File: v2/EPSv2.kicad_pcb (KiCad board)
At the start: 4 copper layers, 50 x 110 mm, 155 parts, among them J1 Conn_01x02, J10 Conn_01x05_Pin, J2 Conn_01x03, J3 Conn_01x03, J4 5037630491, J5 2P 21700 Cell Holder, J6 5037630491, J7 1053091102, J8 1053091102, J9 1053091102, Q1 AO3400A, Q2 AO3400A, Q3 AO3400A, Q4 AO3400A, Q5 AP25P06K, Q6 AP25P06K, Q7 AP25P06K, U1 BQ29700DSER, U10 C3235556 (M66200DRLR), U11 C3235556 (M66200DRLR), U12 TPS63070RNMR, U13 TPS63070RNMR, U14 20m 1206, U15 INA199A1DCKR, U16 20m 1206, U17 INA199A1DCKR, U18 20m 1206, U19 INA199A1DCKR, U2 BQ29700DSER, U20 TPS63070RNMR, U3 MCP73831T-2ACI/OT, U4 MCP73831T-2ACI/OT, U6 C3235556 (M66200DRLR), U7 C3235556 (M66200DRLR), U8 C3235556 (M66200DRLR), U9 STM32L432KCUx

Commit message: preliminary layout
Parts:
- moved L1 202.9 mm to (-11.8, -3.02)
- moved C1 202.9 mm to (-13.9, 2.40)
- moved C10 202.9 mm to (-9.86, 13.1)
- moved C2 202.9 mm to (-13.9, 5.08)
- moved C3 202.9 mm to (-13.9, 7.76)
- moved C4 202.9 mm to (-13.9, 10.4)
- moved C5 202.9 mm to (-13.9, 13.1)
- moved C6 202.9 mm to (-9.86, 2.40)
- moved C7 202.9 mm to (-9.86, 5.08)
- moved C8 202.9 mm to (-9.86, 7.76)
- moved C9 202.9 mm to (-9.86, 10.4)
- moved TP7 139.3 mm to (-4.57, 20.2)
- moved U15 123.4 mm to (3.30, -40.9), turned to 180 degrees
- moved R1 123.4 mm to (-22.1, -10.3)
- moved R2 123.4 mm to (-22.1, -7.80)
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- renumbered J2 to J1, J3 to J2, J1 to J3, U14 to L4, U16 to L5, U18 to L6, L4 to L7, R21 to R20, R22 to R21, R23 to R22, R26 to R23, R27 to R24, R28 to R25, R29 to R26, R30 to R27, R31 to R28, R32 to R29, R33 to R30, R34 to R31, R35 to R32, R36 to R33, R37 to R34, R38 to R35, R39 to R36, R40 to R37, R41 to R38, R42 to R39, R43 to R40, R44 to R41, R45 to R42, R46 to R43, R47 to R44, R48 to R45, R49 to R46, R50 to R47, U11 to U10, U12 to U11, U13 to U12, U15 to U13, U17 to U14, U19 to U15, U20 to U16, U6 to U5, U7 to U6, U8 to U7, U9 to U8, U10 to U9
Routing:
- net PB0: track 44.6 -> 0.00 mm
- net PB1: track 43.9 -> 0.00 mm
- net GND: track 13.9 -> 0.00 mm
- net /Reverse_Polarity/VIN: track 2.24 -> 10.1 mm
- net /MCP73831_1/+5V_VIN: track 14.6 -> 21.7 mm
- net Net-(U2-BAT): track 5.77 -> 0.00 mm
- net Net-(Q4-G): track 5.59 -> 0.00 mm
- net CELL_2-: track 6.93 -> 1.75 mm
- net Net-(U16-EN): track 0.00 -> 3.80 mm
- net Net-(Q3-G): track 3.58 -> 0.00 mm
- net Net-(D1-A): track 3.97 -> 7.48 mm
- net Net-(LED6-A): track 0.00 -> 3.48 mm
- net /INA199_3/IN+: track 0.00 -> 2.50 mm
- net Net-(U16-Vaux): track 0.00 -> 2.15 mm
- net /INA199_3/IN-: track 0.00 -> 2.14 mm
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- added copper zone on F.Cu, net +5V
- added copper zone on F.Cu, net +9V
- added copper zone on F.Cu, net /INA199_1/IN+
- added copper zone on F.Cu, net /INA199_2/IN+
- added copper zone on F.Cu, net /INA199_3/IN+
- added copper zone on F.Cu, net CELL_1-
- added copper zone on F.Cu, net CELL_2-
- added copper zone on F.Cu, net Net-(Q1-D)
- added copper zone on F.Cu, net Net-(Q1-G)
- added copper zone on F.Cu, net Net-(Q2-G)
- added copper zone on F.Cu, net Net-(Q3-D)
- added copper zone on F.Cu, net Net-(Q3-G)
- added copper zone on F.Cu, net Net-(Q4-G)
- added copper zone on F.Cu, net Net-(U1-BAT)
- added copper zone on F.Cu, net Net-(U1-V-)
- added copper zone on F.Cu, net Net-(U12-FB)
- added copper zone on F.Cu, net Net-(U12-L1)
- added copper zone on F.Cu, net Net-(U12-L2)
- added copper zone on F.Cu, net Net-(U16-FB)
- added copper zone on F.Cu, net Net-(U16-L1)
- added copper zone on F.Cu, net Net-(U16-L2)
- added copper zone on F.Cu, net Net-(U2-BAT)
- added copper zone on F.Cu, net Net-(U2-V-)
- removed copper zone on F.Cu, net Net-(U11-FB)
- removed copper zone on F.Cu, net Net-(U11-L1)
- removed copper zone on F.Cu, net Net-(U11-L2)

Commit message: battery charging routing
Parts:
- removed the C10 at (-9.86, 13.1)
- removed the C3 at (-13.9, 7.76)
- removed the C4 at (-13.9, 10.4)
- removed the C5 at (-13.9, 13.1)
- removed the C6 at (-9.86, 2.40)
- removed the C7 at (-9.86, 5.08)
- removed the C8 at (-9.86, 7.76)
- removed the C9 at (-9.86, 10.4)
- added G***: LOGO, Rocketry_Manual:RocketryLogo, F.Cu at (-20.8, -26.2)
- C1, C2: value 10uF 0603 -> 47uF; footprint Rocketry_Easyeda:C0603 -> Capacitor_SMD:C_0603_1608Metric
- moved TP3 124.5 mm to (2.54, 4.06)
- moved TP4 111.7 mm to (15.0, 4.06)
- moved J10 50.4 mm to (-11.2, 51.3), turned to 90 degrees
- moved R21 45.3 mm to (15.2, 6.96), turned to 180 degrees
- moved U6 45.0 mm to (15.1, 9.25), turned to -90 degrees
- moved R20 34.0 mm to (2.55, 6.97), turned to 180 degrees
- moved U5 33.6 mm to (2.42, 9.27), turned to -90 degrees
- moved C22 23.0 mm to (-19.6, 12.1)
- moved C23 23.0 mm to (-17.8, 12.1)
- moved C25 23.0 mm to (-13.7, 18.6)
- moved C28 23.0 mm to (-11.7, 12.2)
- moved L3 23.0 mm to (-15.0, 11.6)
- moved R33 23.0 mm to (-17.8, 15.3)
- moved R35 23.0 mm to (-10.9, 15.5)
- moved R36 23.0 mm to (-15.8, 18.6)
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- renumbered C18 to C10, C19 to C11, C20 to C12, C21 to C13, C22 to C14, C23 to C15, C24 to C16, C25 to C17, C26 to C18, C27 to C19, C28 to C20, C29 to C21, C30 to C22, C31 to C23, C32 to C24, C33 to C25, C34 to C26, C35 to C27, C36 to C28, C37 to C29, C11 to C3, C38 to C30, C39 to C31, C40 to C32, C41 to C33, C42 to C34, C43 to C35, C44 to C36, C45 to C37, C46 to C38, C12 to C4, C13 to C5, C14 to C6, C15 to C7, C16 to C8, C17 to C9
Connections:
- C1 pad 1: GND -> +3.3V
- C1 pad 2: +3.3V -> GND
- C2 pad 1: GND -> /STM32L432KCUx/+3V3A
- C2 pad 2: +3.3V -> GND
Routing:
- net GND: track 0.00 -> 30.8 mm, vias 0 -> 13
- net /STM32L432KCUx/+3V3A: track 0.00 -> 11.5 mm
- net /MCP73831_1/+5V_VIN: track 21.7 -> 13.5 mm
- net /BQ29700_2/CELL+: track 4.84 -> 1.88 mm, vias 0 -> 18
- net PA0: track 0.00 -> 2.94 mm, vias 0 -> 1
- net PA1: track 0.00 -> 2.63 mm, vias 0 -> 1
- net +3.3V: track 1.74 -> 3.48 mm
- net Net-(U5-ST): track 0.00 -> 1.65 mm
- net Net-(U6-ST): track 0.00 -> 1.64 mm
- net /LM66200_2/VOUT: track 7.41 -> 8.69 mm
- net /INA199_2/IN+: track 0.00 -> 1.28 mm
- net /BQ29700_1/CELL+: track 4.84 -> 5.30 mm, vias 0 -> 18
- net CELL_2+: vias 0 -> 12
- net CELL_1+: vias 0 -> 12
- net /INA199_1/IN-: vias 0 -> 4
- added copper zone on B.Cu, net /BQ29700_1/CELL+
- added copper zone on F.Cu, net /BQ29700_1/CELL+
- added copper zone on B.Cu, net /BQ29700_2/CELL+
- added copper zone on F.Cu, net /BQ29700_2/CELL+
- added copper zone on B.Cu, net /INA199_1/IN-
- added copper zone on F.Cu, net /INA199_1/IN-
- added copper zone on F.Cu, net /MCP73831_1/+5V_VIN
- added copper zone on B.Cu, net CELL_1+
- added copper zone on B.Cu, net CELL_2+
- added copper zone on B.Cu, net GND
- added copper zone on F.Cu, net GND
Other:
- board text added: "+3.3V"
- board text added: "+9V"
- board text added: "EPS v2"
- board text added: "McMaster Rocketry"

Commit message: routing done
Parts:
- removed the C29 at (-19.3, -38.1)
- removed the C30 at (-3.32, -38.1)
- removed the L4 at (-16.5, -39.6)
- removed L5, L6: 20m 1206, Rocketry_Easyeda:R1206
- removed the R24 at (2.27, -35.5)
- removed the R25 at (10.0, -35.5)
- removed the R5 at (-16.3, -33.5)
- removed the R6 at (-0.27, -33.5)
- removed the R7 at (7.62, -33.5)
- removed the U10 at (7.49, -35.5)
- removed the U13 at (-19.3, -40.4)
- removed U14, U15: INA199A1DCKR, Rocketry_Easyeda:SC-70-6_L2.2-W1.3-P0.65-LS2.1-BR
- removed the U7 at (-16.4, -35.6)
- removed the U9 at (-0.39, -35.5)
- added C10: 5n, Capacitor_SMD:C_0402_1005Metric, F.Cu at (-22.7, -33.4)
- added C32: 5n, Capacitor_SMD:C_0402_1005Metric, F.Cu at (-12.0, -25.0)
- added C33: 1u / 20V, Capacitor_SMD:C_0402_1005Metric, F.Cu at (1.15, -30.9)
- added C34: 5n, Capacitor_SMD:C_0402_1005Metric, F.Cu at (-3.17, -37.4)
- added C9: 1u / 20V, Capacitor_SMD:C_0402_1005Metric, F.Cu at (-18.3, -26.9)
- added D1: DDZ9678-7, Rocketry_Easyeda:SOD-123_L2.7-W1.6-LS3.7-RD, F.Cu at (-22.5, -29.3)
- added D2: 1N5819WS, Diode_SMD:D_SOD-323, F.Cu at (-18.7, -35.8)
- added D4: DDZ9678-7, Rocketry_Easyeda:SOD-123_L2.7-W1.6-LS3.7-RD, F.Cu at (-11.9, -21.0)
- added D5: 1N5819WS, Diode_SMD:D_SOD-323, F.Cu at (-8.05, -27.5)
- added D6: DDZ9678-7, Rocketry_Easyeda:SOD-123_L2.7-W1.6-LS3.7-RD, F.Cu at (-3.04, -33.3)
- added D7: 1N5819WS, Diode_SMD:D_SOD-323, F.Cu at (0.77, -39.8)
- added JP1: SolderJumper_2_Open, Jumper:SolderJumper-2_P1.3mm_Open_TrianglePad1.0x1.5mm, F.Cu at (-19.6, -29.0)
- added JP2: SolderJumper_2_Open, Jumper:SolderJumper-2_P1.3mm_Open_TrianglePad1.0x1.5mm, F.Cu at (-8.94, -20.6)
- added JP3: SolderJumper_2_Open, Jumper:SolderJumper-2_P1.3mm_Open_TrianglePad1.0x1.5mm, F.Cu at (-0.12, -32.9)
- added R17: 470k, Resistor_SMD:R_0402_1005Metric, F.Cu at (-17.1, -30.2)
- added R18: 220k, Resistor_SMD:R_0402_1005Metric, F.Cu at (-15.9, -31.9)
- added R19: 100k, Resistor_SMD:R_0402_1005Metric, F.Cu at (-15.9, -33.0)
- added R20: 1k, Resistor_SMD:R_0402_1005Metric, F.Cu at (-22.9, -32.3)
- added R21: 1k, Resistor_SMD:R_0402_1005Metric, F.Cu at (-17.6, -33.8)
- added R23: 33k, Resistor_SMD:R_0402_1005Metric, F.Cu at (-15.9, -34.2)
- added R39: 470k, Resistor_SMD:R_0402_1005Metric, F.Cu at (-6.40, -21.9)
- added R40: 220k, Resistor_SMD:R_0402_1005Metric, F.Cu at (-5.25, -23.5)
- added R41: 100k, Resistor_SMD:R_0402_1005Metric, F.Cu at (-5.25, -24.7)
- added R42: 1k, Resistor_SMD:R_0402_1005Metric, F.Cu at (-12.2, -23.9)
- added R43: 1k, Resistor_SMD:R_0402_1005Metric, F.Cu at (-6.90, -25.4)
- added R44: 47k, Resistor_SMD:R_0402_1005Metric, F.Cu at (-8.68, -25.7)
- added R45: 33k, Resistor_SMD:R_0402_1005Metric, F.Cu at (-5.25, -25.8)
- added R46: 470k, Resistor_SMD:R_0402_1005Metric, F.Cu at (2.42, -34.2)
- added R47: 220k, Resistor_SMD:R_0402_1005Metric, F.Cu at (3.56, -35.9)
- added R48: 100k, Resistor_SMD:R_0402_1005Metric, F.Cu at (3.56, -37.0)
- added R49: 1k, Resistor_SMD:R_0402_1005Metric, F.Cu at (-3.37, -36.2)
- added R50: 1k, Resistor_SMD:R_0402_1005Metric, F.Cu at (1.91, -37.8)
- added R51: 47k, Resistor_SMD:R_0402_1005Metric, F.Cu at (0.13, -38.0)
- added R52: 33k, Resistor_SMD:R_0402_1005Metric, F.Cu at (3.56, -38.1)
- added U11: LM73100RPWR, Rocketry_Easyeda:VQFN-10_L2.0-W2.0-P0.45-TL, F.Cu at (-9.09, -23.6)
- added U12: LM73100RPWR, Rocketry_Easyeda:VQFN-10_L2.0-W2.0-P0.45-TL, F.Cu at (-0.28, -35.9)
- added U5: LM73100RPWR, Rocketry_Easyeda:VQFN-10_L2.0-W2.0-P0.45-TL, F.Cu at (-19.8, -31.9)
- C31: value 100nF 0603 -> 1u / 20V; footprint Rocketry_Easyeda:C0603 -> Capacitor_SMD:C_0402_1005Metric
- J10: moved to B.Cu
- R22: value 100k 0603 -> 47k; footprint Rocketry_Easyeda:R0603 -> Resistor_SMD:R_0402_1005Metric
- moved C24 23.8 mm to (3.70, 17.3), turned to 180 degrees
- moved C31 23.0 mm to (-7.67, -18.6), turned to 0 degrees
- moved C25 22.6 mm to (3.70, 19.1), turned to 180 degrees
- moved L3 21.7 mm to (4.13, 21.9), turned to 90 degrees
- moved C28 20.3 mm to (3.54, 29.2), turned to 180 degrees
- moved C26 20.2 mm to (0.57, 17.3), turned to 0 degrees
- moved TP5 20.2 mm to (2.54, 32.0), turned to -90 degrees
- moved C30 20.0 mm to (3.54, 25.2), turned to 180 degrees
- moved C29 20.0 mm to (3.54, 27.2), turned to 180 degrees
- moved R34 18.7 mm to (0.51, 19.1), turned to 0 degrees
- moved U10 17.0 mm to (0.66, 21.9), turned to -90 degrees
- moved C17 16.7 mm to (20.3, 17.3), turned to 180 degrees
- moved C18 16.5 mm to (17.2, 17.3), turned to 0 degrees
- moved R36 15.3 mm to (0.25, 25.9), turned to 90 degrees
- moved LED5 15.0 mm to (-1.27, 31.5), turned to 0 degrees
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- renumbered C9 to C11, C10 to C12, C11 to C13, C12 to C14, C13 to C15, C14 to C16, C15 to C17, C16 to C18, C17 to C19, C18 to C20, C19 to C21, C20 to C22, C21 to C23, C22 to C24, C23 to C25, C24 to C26, C25 to C27, C26 to C28, C27 to C29, C28 to C30, C32 to C35, C33 to C36, C34 to C37, C35 to C38, C36 to C39, C37 to C40, C38 to C41, D1 to D3, D2 to D8, D3 to D9, L7 to L4, R13 to R10, R14 to R11, R15 to R12, R16 to R13, R17 to R14, R18 to R15, R19 to R16, R20 to R24, R21 to R25, R23 to R26, R26 to R27, R27 to R28, R28 to R29, R29 to R30, R30 to R31, R31 to R32, R32 to R33, R33 to R34, R34 to R35, R35 to R36, R36 to R37, R37 to R38, R8 to R5, R38 to R53, R39 to R54, R40 to R55, R41 to R56, R42 to R57, R43 to R58, R44 to R59, R9 to R6, R45 to R60, R46 to R61, R47 to R62, R10 to R7, R11 to R8, R12 to R9, U12 to U10, U16 to U13, U5 to U6, U6 to U7, U11 to U9
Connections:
- net PB0 renamed TEMP_1
- net PB1 renamed TEMP_2
- C31 pad 1: GND -> +5V
- C31 pad 2: +3.3V -> GND
- J7 pad 1: /INA199_1/IN- -> /LM7310_9V/VOUT
- J8 pad 1: /INA199_2/IN- -> /LM7310_5V/VOUT
- J9 pad 1: /INA199_3/IN- -> /LM7310_3.3V/VOUT
- R22 pad 1: Net-(U7-ST) (its old number) -> /LM7310_9V/VOUT
- R22 pad 2: +9V -> Net-(U5-PGTH)
- U8 pad 10: INA199_3 -> LM7310_IOUT_3
- U8 pad 26: unconnected-(U8-PB3-Pad26) -> +3.3V_PG
- U8 pad 27: unconnected-(U8-PB4-Pad27) -> +5V_PG
- U8 pad 28: unconnected-(U8-PB5-Pad28) -> +9V_PG
- U8 pad 29: unconnected-(U8-PB6-Pad29) -> /STM32L432KCUx/PB6
- U8 pad 30: unconnected-(U8-PB7-Pad30) -> /STM32L432KCUx/PB7
- U8 pad 8: INA199_1 -> LM7310_IOUT_1
- U8 pad 9: INA199_2 -> LM7310_IOUT_2
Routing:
- net GND: track 30.8 -> 153.2 mm, vias 13 -> 81
- net ~{MCU_LS_2}: track 0.00 -> 80.2 mm, vias 0 -> 2
- net TEMP_2: track 0.00 -> 76.2 mm, vias 0 -> 2
- net /STM32L432KCUx/nRST: track 0.00 -> 64.0 mm, vias 0 -> 2
- net TEMP_1: track 0.00 -> 62.4 mm, vias 0 -> 2
- net /STM32L432KCUx/SWDCLK: track 0.00 -> 59.3 mm, vias 0 -> 1
- net /STM32L432KCUx/SWDIO: track 0.00 -> 56.5 mm, vias 0 -> 1
- net CELL_2-: track 1.75 -> 54.7 mm, vias 0 -> 6
- net CELL_1-: track 1.75 -> 54.1 mm, vias 0 -> 6
- net ~{MCU_LS_3}: track 1.30 -> 53.2 mm, vias 0 -> 2
- net LM7310_IOUT_3: track 0.00 -> 47.2 mm, vias 0 -> 2
- net +3.3V_PG: track 0.00 -> 45.9 mm, vias 0 -> 2
- net ~{MCU_LS_1}: track 0.00 -> 44.9 mm, vias 0 -> 2
- net LM7310_IOUT_1: track 0.00 -> 42.0 mm, vias 0 -> 2
- net +9V_PG: track 0.00 -> 35.7 mm, vias 0 -> 2
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- added copper zone on In1.Cu, net +3.3V
- added copper zone on In1.Cu, net +5V
- added copper zone on B.Cu, net +9V
- added copper zone on B.Cu, net /LM7310_3.3V/VOUT
- added copper zone on F.Cu, net /LM7310_3.3V/VOUT
- added copper zone on B.Cu, net /LM7310_5V/VOUT
- added copper zone on F.Cu, net /LM7310_5V/VOUT
- added copper zone on B.Cu, net /LM7310_9V/VOUT
- added copper zone on F.Cu, net /LM7310_9V/VOUT
- added copper zone on In2.Cu, net CELL_1-
- added copper zone on In2.Cu, net CELL_2-
- added copper zone on F.Cu, net Net-(U9-L1)
- added copper zone on F.Cu, net Net-(U9-L2)
- removed copper zone on F.Cu, net /INA199_1/IN+
- removed copper zone on B.Cu, net /INA199_1/IN-
- removed copper zone on F.Cu, net /INA199_1/IN-
- removed copper zone on F.Cu, net /INA199_2/IN+
- removed copper zone on F.Cu, net /INA199_3/IN+
- removed copper zone on In1.Cu, net GND
- removed copper zone on F.Cu, net Net-(U10-FB)
- removed copper zone on F.Cu, net Net-(U10-L1)
- removed copper zone on F.Cu, net Net-(U10-L2)
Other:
- board text added: "Designed in Canada"

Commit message: CAN txrx
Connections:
- J4 pad 2: unconnected-(J4-GND-Pad2) -> GND
- J4 pad 3: unconnected-(J4-CANH-Pad3) -> CAN_TX
- J4 pad 4: unconnected-(J4-CANL-Pad4) -> CAN_RX
- J6 pad 2: unconnected-(J6-GND-Pad2) -> GND
- J6 pad 3: unconnected-(J6-CANH-Pad3) -> CAN_TX
- J6 pad 4: unconnected-(J6-CANL-Pad4) -> CAN_RX
- J7 pad S1: (no net) -> unconnected-(J7-PadS1)
- J7 pad S2: (no net) -> unconnected-(J7-PadS2)
- J8 pad S1: (no net) -> unconnected-(J8-PadS1)
- J8 pad S2: (no net) -> unconnected-(J8-PadS2)
- J9 pad S1: (no net) -> unconnected-(J9-PadS1)
- J9 pad S2: (no net) -> unconnected-(J9-PadS2)
- U8 pad 18: /STM32L432KCUx/PA8 -> unconnected-(U8-PA8-Pad18)
- U8 pad 21: unconnected-(U8-PA11-Pad21) -> CAN_RX
- U8 pad 22: unconnected-(U8-PA12-Pad22) -> CAN_TX
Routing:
- net CAN_TX: track 0.00 -> 69.5 mm, vias 0 -> 2
- net CAN_RX: track 0.00 -> 69.2 mm, vias 0 -> 2
- net ~{MCU_LS_2}: track 80.2 -> 39.9 mm
- net GND: track 153.2 -> 146.5 mm, vias 81 -> 83
- net TEMP_1: track 62.4 -> 59.8 mm
- net TEMP_2: track 76.2 -> 74.4 mm
- net /STM32L432KCUx/SWDCLK: track 59.3 -> 60.8 mm
- net CELL_2+: track 28.2 -> 26.7 mm, vias 15 -> 14
- net /STM32L432KCUx/SWDIO: track 56.5 -> 57.9 mm
- net /LM7310_9V/VOUT: track 11.4 -> 12.2 mm
- net /LM7310_5V/VOUT: track 25.7 -> 25.0 mm
- net /STM32L432KCUx/I2C1_SDA: track 1.19 -> 1.85 mm
- added copper zone on In1.Cu, net +9V
- removed copper zone on B.Cu, net +9V
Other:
- board text added: "+5V"
- board text removed: "+5.0V"

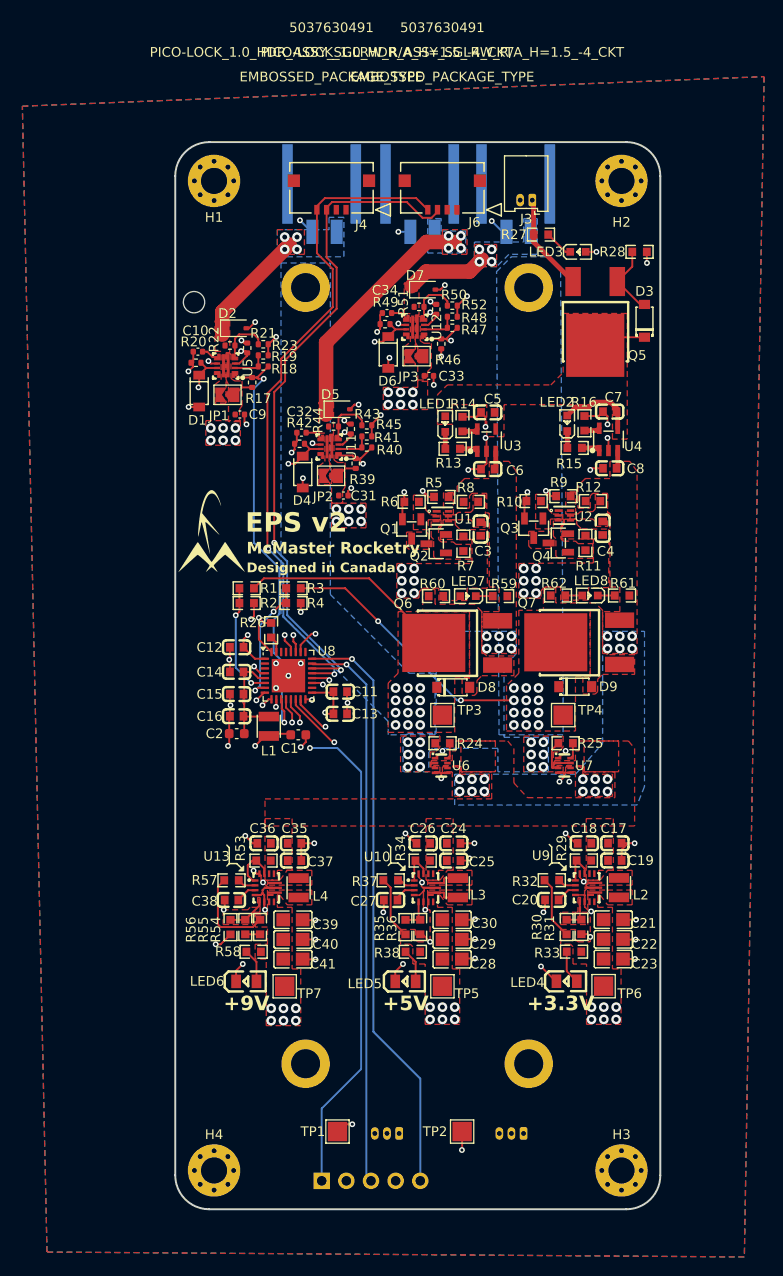
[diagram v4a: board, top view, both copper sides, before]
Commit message: can transceiver and battery reverse polarity bypass
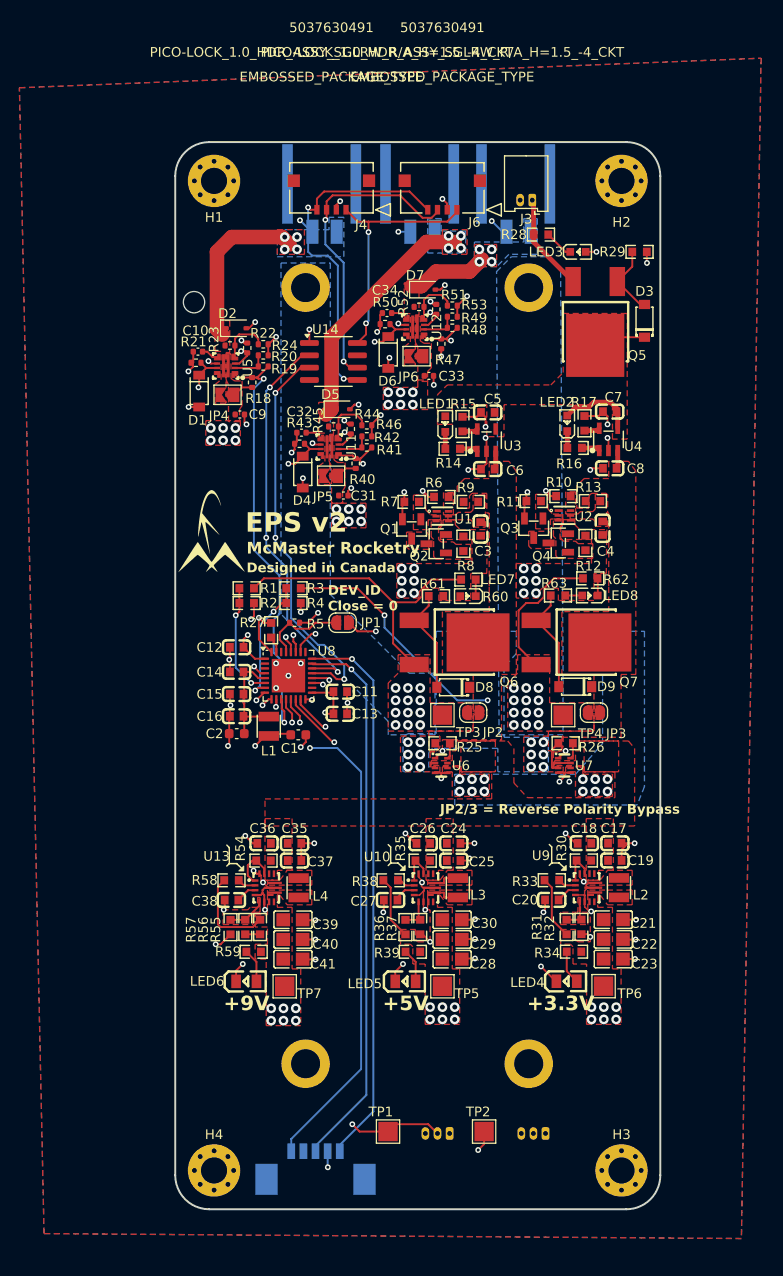
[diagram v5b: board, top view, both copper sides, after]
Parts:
- added JP1: SolderJumper_2_Open, Jumper:SolderJumper-2_P1.3mm_Open_RoundedPad1.0x1.5mm, F.Cu at (-7.75, -5.46)
- added JP2: SolderJumper_2_Open, Jumper:SolderJumper-2_P1.3mm_Open_RoundedPad1.0x1.5mm, F.Cu at (5.71, 3.81)
- added JP3: SolderJumper_2_Open, Jumper:SolderJumper-2_P1.3mm_Open_RoundedPad1.0x1.5mm, F.Cu at (18.2, 3.81)
- added R5: 10k, Resistor_SMD:R_0402_1005Metric, F.Cu at (-12.7, -5.46)
- added U14: ISO1044BD, Package_SO:SOIC-8_3.9x4.9mm_P1.27mm, F.Cu at (-8.70, -32.4)
- J10: footprint Connector_PinHeader_2.54mm:PinHeader_1x05_P2.54mm_Vertical -> Rocketry_Easyeda:CONN-SMD_5P-P1.25_532610571-2
- moved TP1 5.21 mm to (-3.07, 47.0)
- moved J1 5.21 mm to (3.28, 47.2)
- moved R62 3.73 mm to (17.8, -10.0), turned to 180 degrees
- moved R60 3.68 mm to (5.22, -9.91), turned to 180 degrees
- moved J2 2.27 mm to (13.2, 47.2)
- moved TP2 2.27 mm to (6.84, 47.0)
- moved Q7 2.03 mm to (15.5, -3.42), turned to -90 degrees
- moved Q6 2.02 mm to (2.92, -3.43), turned to -90 degrees
- moved J10 1.73 mm to (-10.5, 50.5), turned to 180 degrees
- turned D8 to 180 degrees
- turned D9 to 180 degrees
- renumbered JP1 to JP4, JP2 to JP5, JP3 to JP6, R9 to R10, R10 to R11, R11 to R12, R12 to R13, R13 to R14, R14 to R15, R15 to R16, R16 to R17, R17 to R18, R18 to R19, R19 to R20, R20 to R21, R21 to R22, R22 to R23, R23 to R24, R24 to R25, R25 to R26, R26 to R27, R27 to R28, R28 to R29, R29 to R30, R30 to R31, R31 to R32, R32 to R33, R33 to R34, R34 to R35, R35 to R36, R36 to R37, R37 to R38, R38 to R39, R39 to R40, R40 to R41, R41 to R42, R42 to R43, R43 to R44, R44 to R45, R45 to R46, R46 to R47, R47 to R48, R48 to R49, R49 to R50, R50 to R51, R51 to R52, R52 to R53, R53 to R54, R54 to R55, R55 to R56, R56 to R57, R57 to R58, R58 to R59, R5 to R6, R59 to R60, R60 to R61, R61 to R62, R62 to R63, R6 to R7, R7 to R8, R8 to R9
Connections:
- net PA0 renamed CELL_1_VMON
- net PA1 renamed CELL_2_VMON
- D8 pad 1: CELL_1+ -> /BQ29700_1/CELL+
- D9 pad 1: CELL_2+ -> /BQ29700_2/CELL+
- J4 pad 1: unconnected-(J4-VCC-Pad1) -> Net-(J4-VCC)
- J4 pad 3: CAN_TX -> Net-(J4-CANH)
- J4 pad 4: CAN_RX -> Net-(J4-CANL)
- J6 pad 1: unconnected-(J6-VCC-Pad1) -> Net-(J4-VCC)
- J6 pad 3: CAN_TX -> Net-(J4-CANH)
- J6 pad 4: CAN_RX -> Net-(J4-CANL)
- Q6 pad 2: /BQ29700_1/CELL+ -> CELL_1+
- Q6 pad 3: CELL_1+ -> /BQ29700_1/CELL+
- Q7 pad 2: /BQ29700_2/CELL+ -> CELL_2+
- Q7 pad 3: CELL_2+ -> /BQ29700_2/CELL+
- R60 pad 2: /BQ29700_1/CELL+ -> CELL_1+
- R62 pad 2: /BQ29700_2/CELL+ -> CELL_2+
- U8 pad 29: /STM32L432KCUx/PB6 -> /DEV_ID
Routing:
- net Net-(J4-CANL): track 0.00 -> 36.3 mm, vias 0 -> 2
- net Net-(J4-VCC): track 0.00 -> 33.1 mm, vias 0 -> 3
- net Net-(J4-CANH): track 0.00 -> 32.1 mm, vias 0 -> 2
- net CAN_TX: track 69.5 -> 40.7 mm, vias 2 -> 3
- net CAN_RX: track 69.2 -> 41.0 mm, vias 2 -> 3
- net CELL_2+: track 26.7 -> 42.3 mm
- net Net-(D9-A): track 0.00 -> 11.0 mm
- net Net-(D8-A): track 0.00 -> 11.0 mm
- net CELL_1+: track 21.7 -> 31.5 mm
- net /DEV_ID: track 0.00 -> 9.04 mm
- net GND: track 146.5 -> 152.0 mm, vias 83 -> 86
- net /LM7310_9V/VOUT: track 12.2 -> 17.2 mm
- net +3.3V: track 23.5 -> 27.5 mm, vias 19 -> 21
- net /STM32L432KCUx/SWDCLK: track 60.8 -> 57.2 mm
- net TEMP_1: track 59.8 -> 63.3 mm
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- removed copper zone on F.Cu, net Net-(D8-A)
- removed copper zone on F.Cu, net Net-(D9-A)
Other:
- board text added: "DEV_ID Close = 0"
- board text added: "JP2/3 = Reverse Polarity Bypass"
